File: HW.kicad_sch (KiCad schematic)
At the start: 0 parts

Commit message: WIP: Save before switching
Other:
- sheet LoRA Module ports: added RESET; removed none
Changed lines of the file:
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@@
+	)
+	(bus_entry
+		(at 124.46 110.49)
+		(size -2.54 2.54)
+		(stroke
+			(width 0)
+			(type default)
+		)
 	)
 	(bus_entry
@@
 	(bus
 		(pts
-			(xy 124.46 106.68) (xy 124.46 127)
+			(xy 124.46 106.68) (xy 124.46 110.49)
 		)
 		(stroke
@@
 		)
 	)
+	(bus
+		(pts
+			(xy 124.46 110.49) (xy 124.46 127)
+		)
+		(stroke
+			(width 0)
+			(type default)
+		)
+	)
 	(wire
 		(pts
@@
 		(pts
 			(xy 147.32 54.61) (xy 147.32 58.42)
+		)
+		(stroke
+			(width 0)
+			(type default)
+		)
+	)
+	(wire
+		(pts
+			(xy 106.68 113.03) (xy 121.92 113.03)
 		)
 		(stroke
@@
 			)
 			(justify right bottom)
+		)
+	)
+	(label "RESET"
+		(at 106.68 113.03 0)
+		(effects
+			(font
+				(size 1.27 1.27)
+			)
+			(justify left bottom)
 		)
 	)
@@
 			(effects
 				(font
+					(size 1.27 1.27)
+				)
+				(justify right)
+			)
+		)
+		(pin "RESET" input
+			(at 106.68 113.03 0)
+			(effects
+				(font

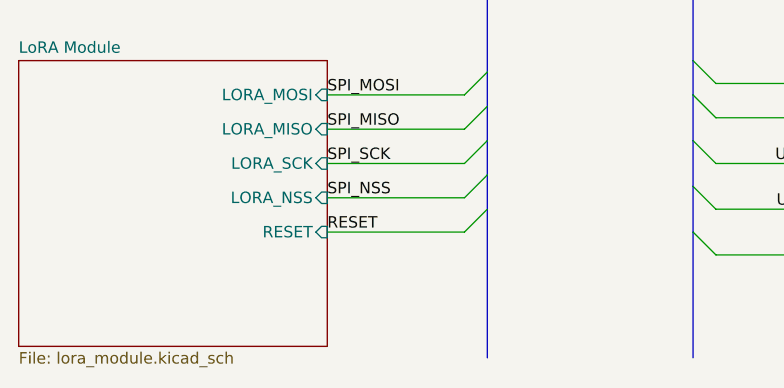
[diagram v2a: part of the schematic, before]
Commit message: fix(main-schematic): connect VCC to bus system for ERC
- Add VCC label and wire connection to power bus
- Extend bus routing to include VCC power net
- Resolves ERC warnings about floating VCC
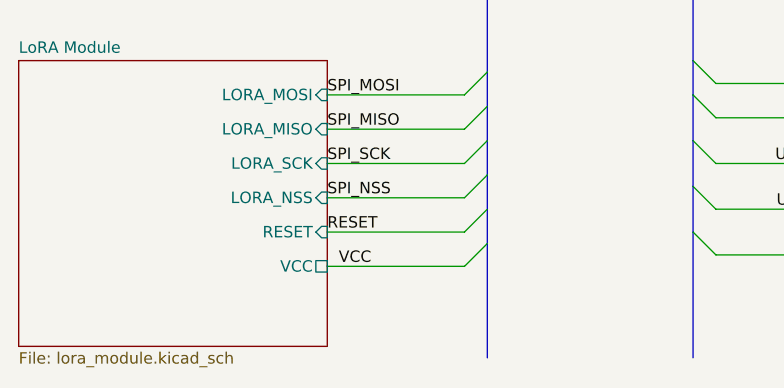
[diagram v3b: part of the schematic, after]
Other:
- sheet LoRA Module ports: added VCC; removed none
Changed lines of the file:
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@@
+	)
+	(bus_entry
+		(at 121.92 116.84)
+		(size 2.54 -2.54)
+		(stroke
+			(width 0)
+			(type default)
+		)
 	)
 	(bus_entry
@@
 		)
 	)
+	(wire
+		(pts
+			(xy 106.68 116.84) (xy 121.92 116.84)
+		)
+		(stroke
+			(width 0)
+			(type default)
+		)
+	)
 	(bus
 		(pts
@@
 	(bus
 		(pts
+			(xy 124.46 114.3) (xy 124.46 127)
+		)
+		(stroke
+			(width 0)
+			(type default)
+		)
+	)
+	(bus
+		(pts
 			(xy 124.46 63.5) (xy 124.46 95.25)
 		)
@@
 	(bus
 		(pts
-			(xy 124.46 110.49) (xy 124.46 127)
+			(xy 124.46 110.49) (xy 124.46 114.3)
 		)
 		(stroke
@@
 			)
 			(justify right bottom)
+		)
+	)
+	(label "VCC "
+		(at 107.95 116.84 0)
+		(effects
+			(font
+				(size 1.27 1.27)
+			)
+			(justify left bottom)
 		)
 	)
@@
 			(effects
 				(font
+					(size 1.27 1.27)
+				)
+				(justify right)
+			)
+		)
+		(pin "VCC" passive
+			(at 106.68 116.84 0)
+			(effects
+				(font

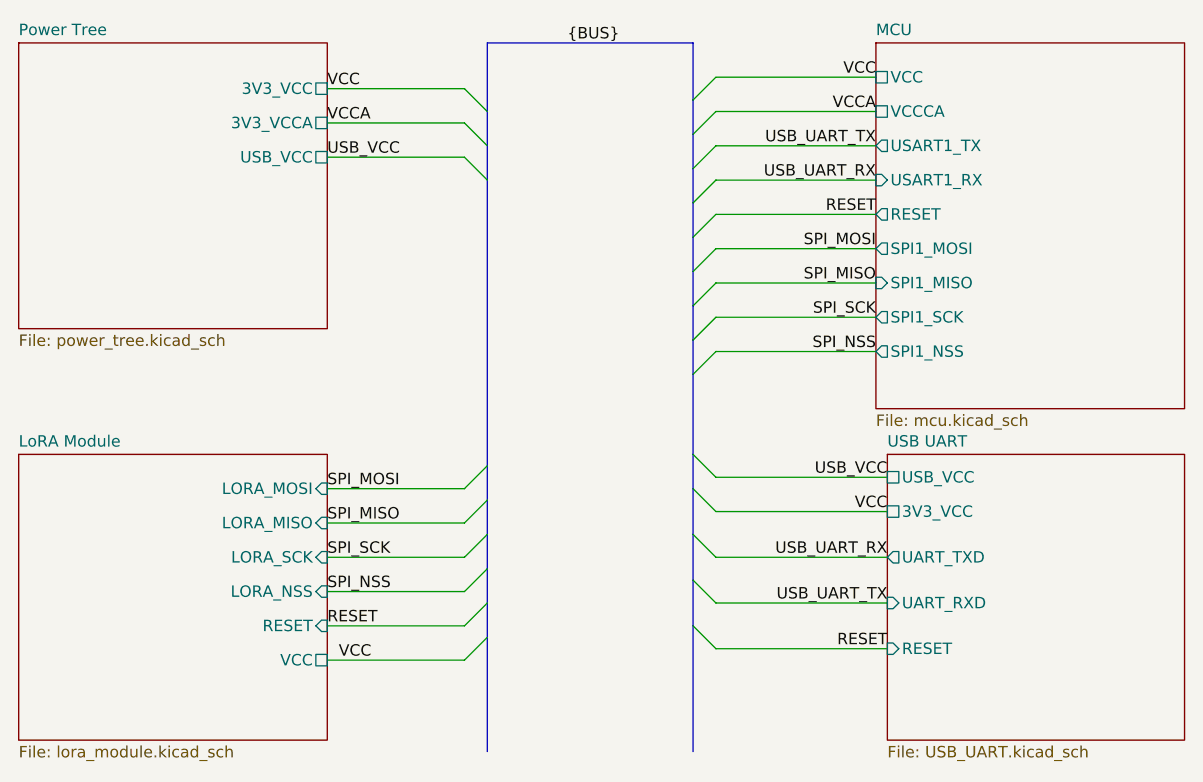
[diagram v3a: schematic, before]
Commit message: refactor(root-sch): relocate bus entries after hierarchical label cleanup
Shifts the bus-entry X-coordinate from 147.32 to 148.59 to realign the bus with the updated sub-sheet layouts, and removes the orphaned bus entries left behind by the dropped VCC/USB_VCC/3V3_VCC/VCCCA hierarchical labels in the power, USB-UART, MCU and LoRa sheets. Downstream consequence of the power-rail refactor.
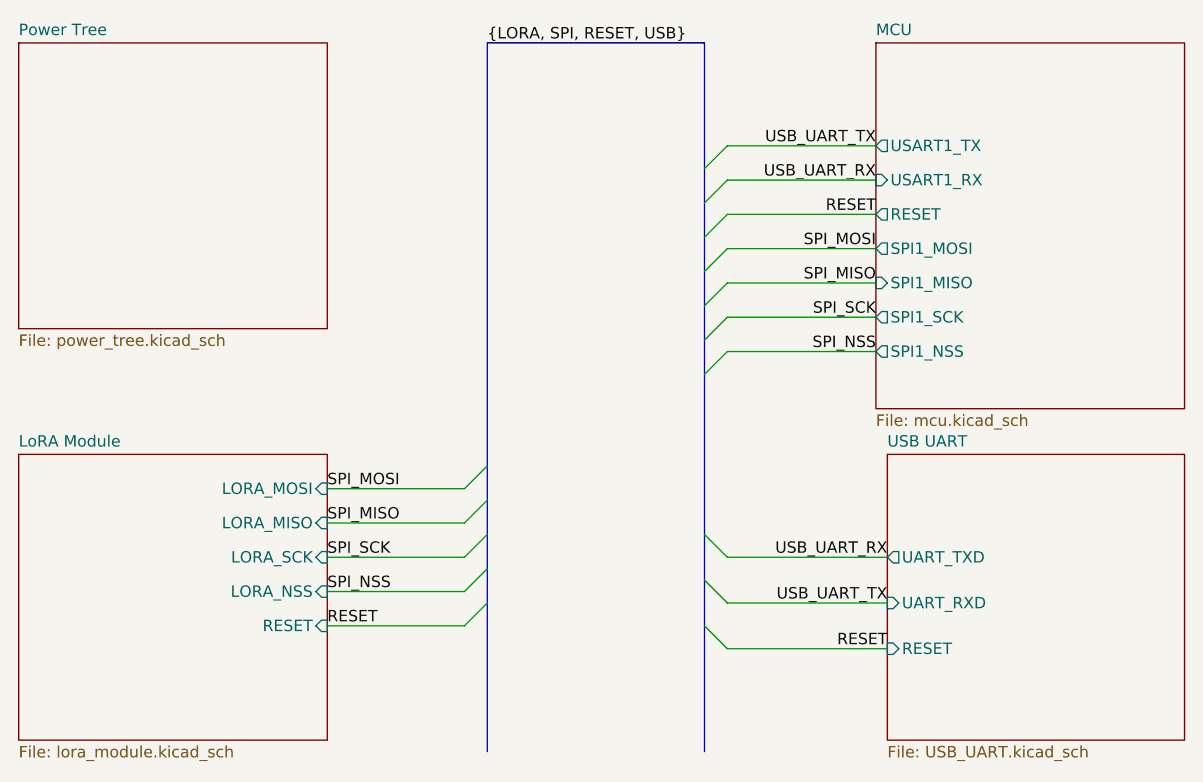
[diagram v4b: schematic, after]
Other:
- sheet LoRA Module ports: added none; removed VCC
- sheet MCU ports: added none; removed VCC, VCCCA
- sheet Power Tree ports: added none; removed 3V3_VCC, 3V3_VCCA, USB_VCC
- sheet USB UART ports: added none; removed 3V3_VCC, USB_VCC
